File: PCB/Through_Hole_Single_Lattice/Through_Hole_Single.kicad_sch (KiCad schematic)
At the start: 33 parts, among them J2 2x20_Conn, Q1 TN2106, Q10 TN2106, Q2 TN2106, Q3 TN2106, Q4 TN2106, Q5 TN2106, Q6 TN2106, Q7 TN2106, Q8 TN2106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

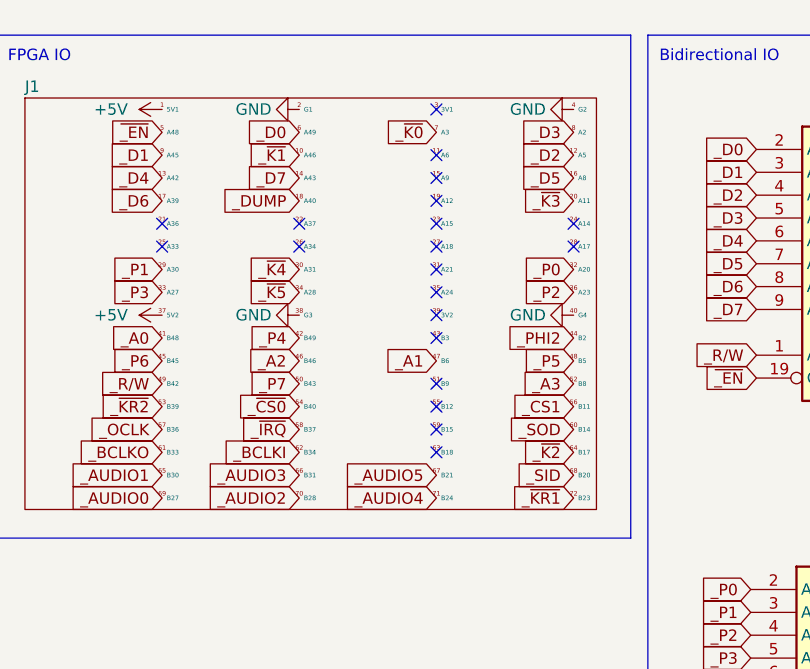
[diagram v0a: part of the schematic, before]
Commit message: Added several new test boards
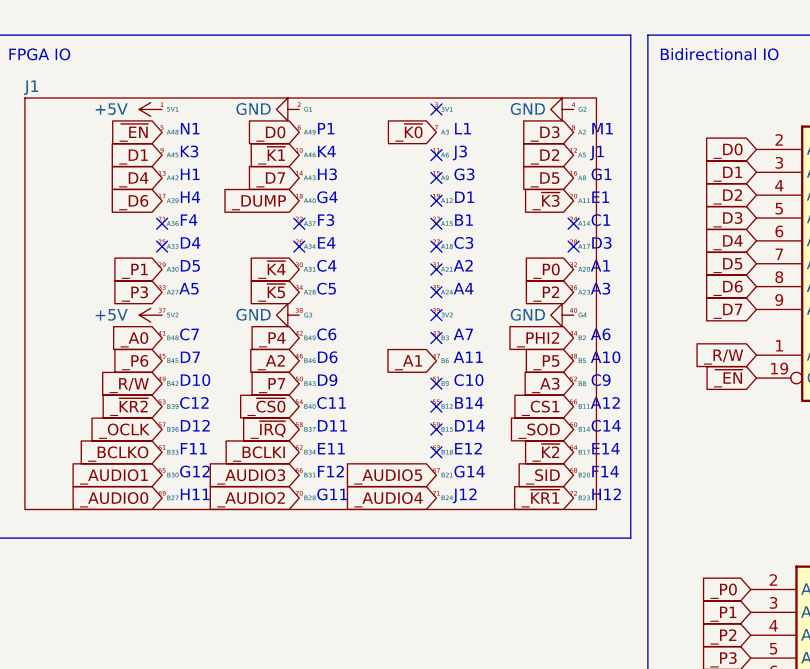
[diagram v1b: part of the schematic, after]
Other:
- note added: "A1"
- note added: "A10"
- note added: "A11"
- note added: "A12"
- note added: "A2"
- note added: "A3"
- note added: "A4"
- note added: "A5"
- note added: "A6"
- note added: "A7"
- note added: "B1"
- note added: "B14"
- note added: "C1"
- note added: "C10"
- note added: "C11"
- note added: "C12"
- note added: "C14"
- note added: "C3"
- note added: "C4"
- note added: "C5"
- note added: "C6"
- note added: "C7"
- note added: "C9"
- note added: "D1"
- note added: "D10"
- note added: "D11"
- note added: "D12"
- note added: "D14"
- note added: "D3"
- note added: "D4"
- note added: "D5"
- note added: "D6"
- note added: "D7"
- note added: "D9"
- note added: "E1"
- note added: "E11"
- note added: "E12"
- note added: "E14"
- note added: "E4"
- note added: "F11"
- note added: "F12"
- note added: "F14"
- note added: "F3"
- note added: "F4"
- note added: "G1"
- note added: "G11"
- note added: "G12"
- note added: "G14"
- note added: "G3"
- note added: "G4"
- note added: "H1"
- note added: "H11"
- note added: "H12"
- note added: "H3"
- note added: "H4"
- note added: "J1"
- note added: "J12"
- note added: "J3"
- note added: "K3"
- note added: "K4"
- note added: "L1"
- note added: "M1"
- note added: "N1"
- note added: "P1"
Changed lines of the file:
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@@
     (fill (type none))
   )
+  (text "F11" (at 89.535 63.5 0)
+    (effects (font (size 1.27 1.27)) (justify left bottom))
+  )
+  (text "D11" (at 104.775 60.96 0)
+    (effects (font (size 1.27 1.27)) (justify left bottom))
+  )
+  (text "E11" (at 104.775 63.5 0)
+    (effects (font (size 1.27 1.27)) (justify left bottom))
+  )
+  (text "H12" (at 135.255 68.58 0)
+    (effects (font (size 1.27 1.27)) (justify left bottom))
+  )
+  (text "D1" (at 120.015 35.56 0)
+    (effects (font (size 1.27 1.27)) (justify left bottom))
+  )
+  (text "C7" (at 89.535 50.8 0)
+    (effects (font (size 1.27 1.27)) (justify left bottom))
+  )
+  (text "A2" (at 120.015 43.18 0)
+    (effects (font (size 1.27 1.27)) (justify left bottom))
+  )
+  (text "D14" (at 120.015 60.96 0)
+    (effects (font (size 1.27 1.27)) (justify left bottom))
+  )
+  (text "F4" (at 89.535 38.1 0)
+    (effects (font (size 1.27 1.27)) (justify left bottom))
+  )
+  (text "C3" (at 120.015 40.64 0)
+    (effects (font (size 1.27 1.27)) (justify left bottom))
+  )
+  (text "D3" (at 135.255 40.64 0)
+    (effects (font (size 1.27 1.27)) (justify left bottom))
+  )
+  (text "L1" (at 120.015 27.94 0)
+    (effects (font (size 1.27 1.27)) (justify left bottom))
+  )
+  (text "C12" (at 89.535 58.42 0)
+    (effects (font (size 1.27 1.27)) (justify left bottom))
+  )
+  (text "D7" (at 89.535 53.34 0)
+    (effects (font (size 1.27 1.27)) (justify left bottom))
+  )
+  (text "D5" (at 89.535 43.18 0)
+    (effects (font (size 1.27 1.27)) (justify left bottom))
+  )
+  (text "A5" (at 89.535 45.72 0)
+    (effects (font (size 1.27 1.27)) (justify left bottom))
+  )
+  (text "C9" (at 135.255 55.88 0)
+    (effects (font (size 1.27 1.27)) (justify left bottom))
+  )
+  (text "E14" (at 135.255 63.5 0)
+    (effects (font (size 1.27 1.27)) (justify left bottom))
+  )
+  (text "C6" (at 104.775 50.8 0)
+    (effects (font (size 1.27 1.27)) (justify left bottom))
+  )
+  (text "A12" (at 135.255 58.42 0)
+    (effects (font (size 1.27 1.27)) (justify left bottom))
+  )
+  (text "M1" (at 135.255 27.94 0)
+    (effects (font (size 1.27 1.27)) (justify left bottom))
+  )
+  (text "D12" (at 89.535 60.96 0)
+    (effects (font (size 1.27 1.27)) (justify left bottom))
+  )
+  (text "C14" (at 135.255 60.96 0)
+    (effects (font (size 1.27 1.27)) (justify left bottom))
+  )
+  (text "B14" (at 120.015 58.42 0)
+    (effects (font (size 1.27 1.27)) (justify left bottom))
+  )
+  (text "D10" (at 89.535 55.88 0)
+    (effects (font (size 1.27 1.27)) (justify left bottom))
+  )
+  (text "E1" (at 135.255 35.56 0)
+    (effects (font (size 1.27 1.27)) (justify left bottom))
+  )
+  (text "J3" (at 120.015 30.48 0)
+    (effects (font (size 1.27 1.27)) (justify left bottom))
+  )
+  (text "C4" (at 104.775 43.18 0)
+    (effects (font (size 1.27 1.27)) (justify left bottom))
+  )
+  (text "J1" (at 135.255 30.48 0)
+    (effects (font (size 1.27 1.27)) (justify left bottom))
+  )
+  (text "B1" (at 120.015 38.1 0)
+    (effects (font (size 1.27 1.27)) (justify left bottom))
+  )
+  (text "A10" (at 135.255 53.34 0)
+    (effects (font (size 1.27 1.27)) (justify left bottom))
+  )
+  (text "H4" (at 89.535 35.56 0)
+    (effects (font (size 1.27 1.27)) (justify left bottom))
+  )
+  (text "J12" (at 120.015 68.58 0)
+    (effects (font (size 1.27 1.27)) (justify left bottom))
+  )
+  (text "D6" (at 104.775 53.34 0)
+    (effects (font (size 1.27 1.27)) (justify left bottom))
+  )
+  (text "G4" (at 104.775 35.56 0)
+    (effects (font (size 1.27 1.27)) (justify left bottom))
+  )
+  (text "D4" (at 89.535 40.64 0)
+    (effects (font (size 1.27 1.27)) (justify left bottom))
+  )
+  (text "G1" (at 135.255 33.02 0)
+    (effects (font (size 1.27 1.27)) (justify left bottom))
+  )
+  (text "D9" (at 104.775 55.88 0)
+    (effects (font (size 1.27 1.27)) (justify left bottom))
+  )
   (text "Unidirectional IO" (at 191.77 17.78 0)
     (effects (font (size 1.27 1.27)) (justify left bottom))
   )
+  (text "G14" (at 120.015 66.04 0)
+    (effects (font (size 1.27 1.27)) (justify left bottom))
+  )
   (text "Arcade PCB Interface" (at 24.765 19.685 0)
     (effects (font (size 1.27 1.27)) (justify left bottom))
   )
+  (text "A7" (at 120.015 50.8 0)
+    (effects (font (size 1.27 1.27)) (justify left bottom))
+  )
+  (text "C11" (at 104.775 58.42 0)
+    (effects (font (size 1.27 1.27)) (justify left bottom))
+  )
+  (text "H11" (at 89.535 68.58 0)
+    (effects (font (size 1.27 1.27)) (justify left bottom))
+  )
+  (text "C1" (at 135.255 38.1 0)
+    (effects (font (size 1.27 1.27)) (justify left bottom))
+  )
+  (text "K3" (at 89.535 30.48 0)
+    (effects (font (size 1.27 1.27)) (justify left bottom))
+  )
+  (text "A6" (at 135.255 50.8 0)
+    (effects (font (size 1.27 1.27)) (justify left bottom))
+  )
+  (text "G12" (at 89.535 66.04 0)
+    (effects (font (size 1.27 1.27)) (justify left bottom))
+  )
   (text "Bidirectional IO" (at 142.875 19.685 0)
     (effects (font (size 1.27 1.27)) (justify left bottom))
   )
+  (text "C5" (at 104.775 45.72 0)
+    (effects (font (size 1.27 1.27)) (justify left bottom))
+  )
+  (text "E4" (at 104.775 40.64 0)
+    (effects (font (size 1.27 1.27)) (justify left bottom))
+  )
+  (text "G3" (at 120.015 33.02 0)
+    (effects (font (size 1.27 1.27)) (justify left bottom))
+  )
+  (text "F12" (at 104.775 66.04 0)
+    (effects (font (size 1.27 1.27)) (justify left bottom))
+  )
   (text "Audio Output" (at 18.415 131.445 0)
     (effects (font (size 1.27 1.27)) (justify left bottom))
   )
+  (text "A1" (at 135.255 43.18 0)
+    (effects (font (size 1.27 1.27)) (justify left bottom))
+  )
+  (text "F14" (at 135.255 66.04 0)
+    (effects (font (size 1.27 1.27)) (justify left bottom))
+  )
+  (text "G11" (at 104.775 68.58 0)
+    (effects (font (size 1.27 1.27)) (justify left bottom))
+  )
+  (text "P1" (at 104.775 27.94 0)
+    (effects (font (size 1.27 1.27)) (justify left bottom))
+  )
+  (text "A3" (at 135.255 45.72 0)
+    (effects (font (size 1.27 1.27)) (justify left bottom))
+  )
   (text "Power Supply" (at 17.78 168.91 0)
     (effects (font (size 1.27 1.27)) (justify left bottom))
   )
+  (text "H3" (at 104.775 33.02 0)
+    (effects (font (size 1.27 1.27)) (justify left bottom))
+  )
+  (text "N1" (at 89.535 27.94 0)
+    (effects (font (size 1.27 1.27)) (justify left bottom))
+  )
+  (text "A11" (at 120.015 53.34 0)
+    (effects (font (size 1.27 1.27)) (justify left bottom))
+  )
   (text "Open Drain Outputs" (at 17.78 106.045 0)
     (effects (font (size 1.27 1.27)) (justify left bottom))
   )
+  (text "E12" (at 120.015 63.5 0)
+    (effects (font (size 1.27 1.27)) (justify left bottom))
+  )
+  (text "A4" (at 120.015 45.72 0)
+    (effects (font (size 1.27 1.27)) (justify left bottom))
+  )
   (text "FPGA IO" (at 70.485 19.685 0)
     (effects (font (size 1.27 1.27)) (justify left bottom))
   )
+  (text "K4" (at 104.775 30.48 0)
+    (effects (font (size 1.27 1.27)) (justify left bottom))
+  )
+  (text "H1" (at 89.535 33.02 0)
+    (effects (font (size 1.27 1.27)) (justify left bottom))
+  )
+  (text "C10" (at 120.015 55.88 0)
+    (effects (font (size 1.27 1.27)) (justify left bottom))
+  )
+  (text "F3" (at 104.775 38.1 0)
+    (effects (font (size 1.27 1.27)) (justify left bottom))
+  )
